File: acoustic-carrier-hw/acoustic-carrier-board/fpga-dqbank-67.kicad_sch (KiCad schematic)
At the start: 11 parts, among them IC1 ECP5-BGA256, Y601 Crystal Oscillator

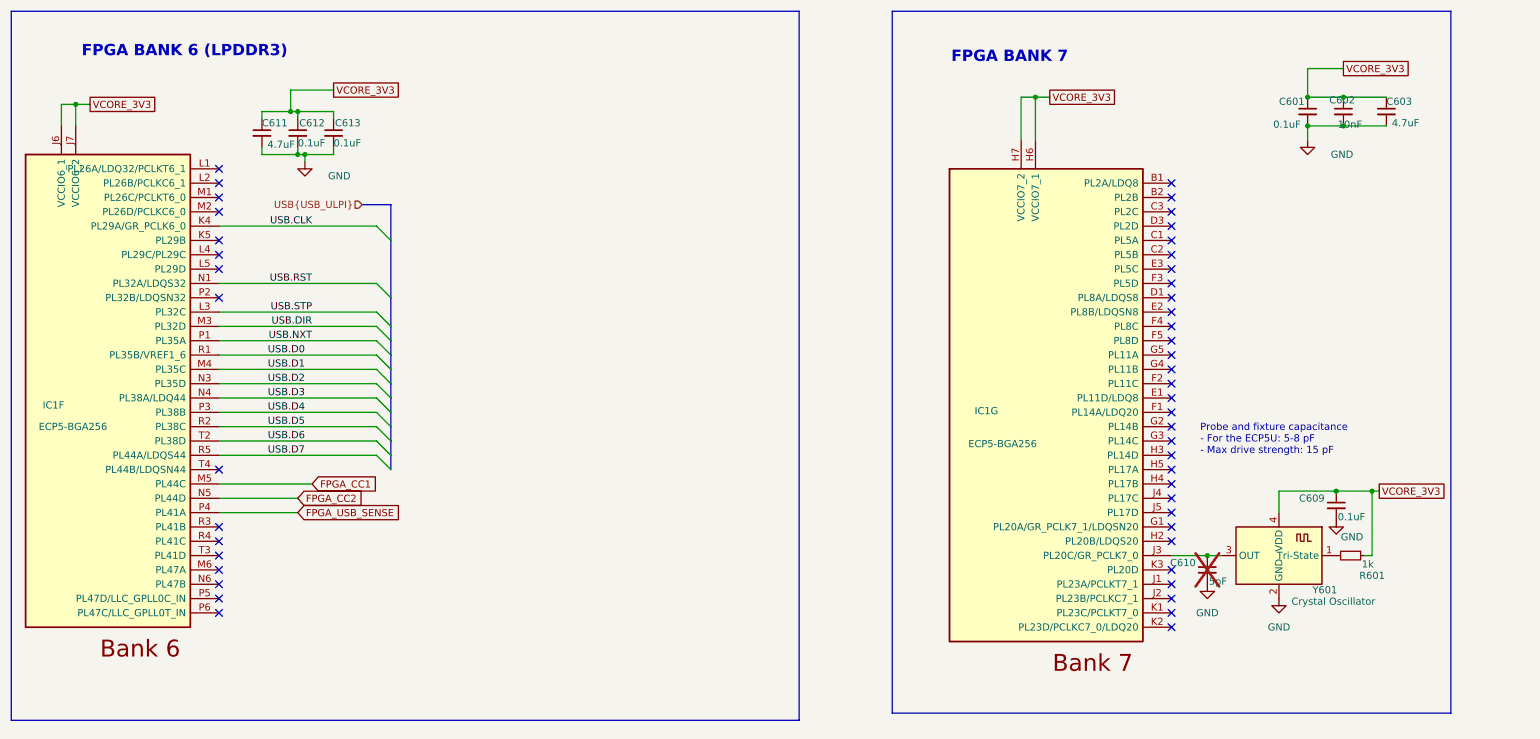
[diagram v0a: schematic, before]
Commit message: [carrier] connected ethernet, usb and adc to appropriate banks, redpositioned schmitt trigger and USB
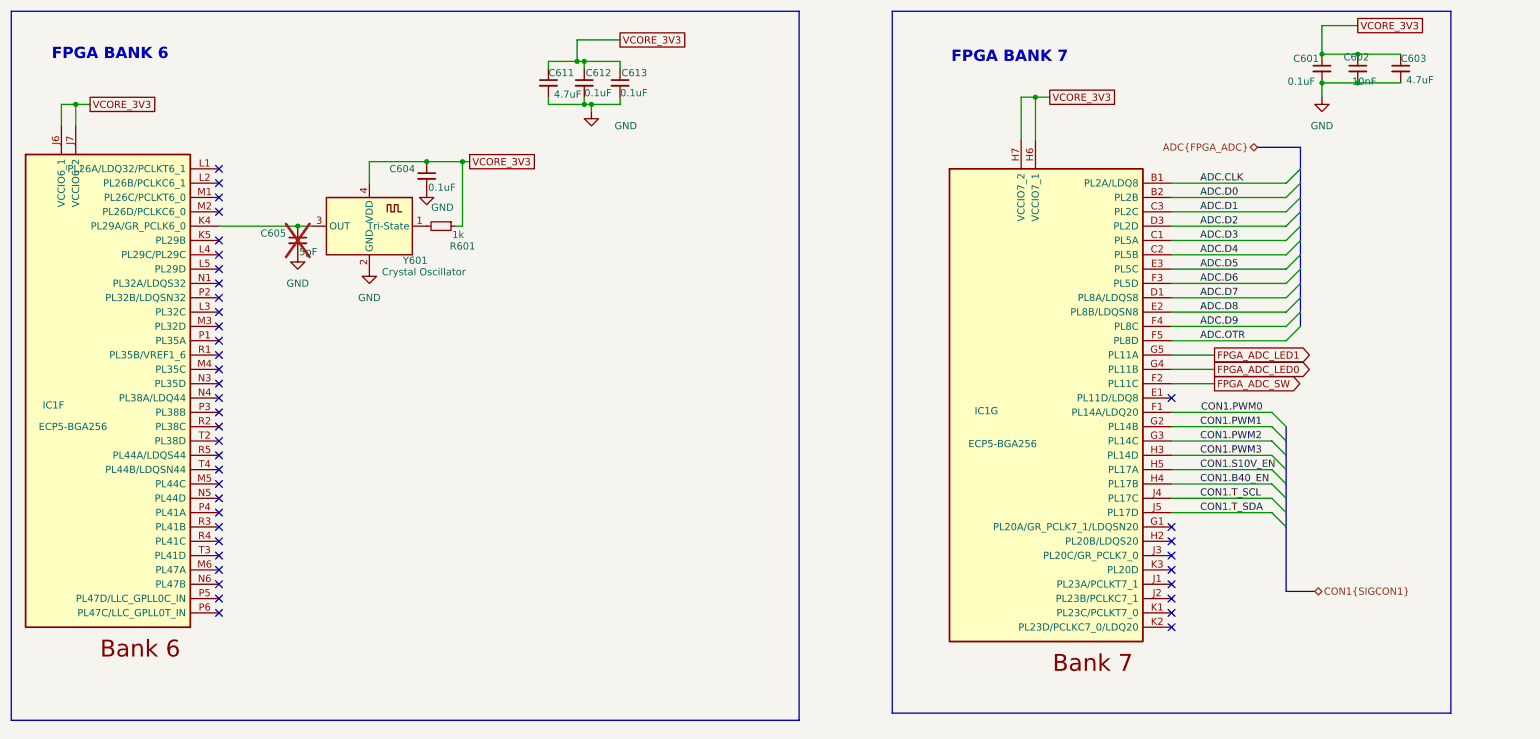
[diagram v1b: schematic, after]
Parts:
- removed C609: 0.1uF, Capacitor_SMD:C_0201_0603Metric, symbol Device:C_Small
- removed C610: 5pF, Capacitor_SMD:C_0603_1608Metric, symbol Device:C_Small
- added C604: 0.1uF, Capacitor_SMD:C_0201_0603Metric, symbol Device:C_Small
- added C605: 5pF, Capacitor_SMD:C_0603_1608Metric, symbol Device:C_Small
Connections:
- net USB.CLK is gone; now on an unnamed net: IC1.K4 (PL29A/GR_PCLK6_0)
- net GND: now also C604.2, C605.2
- net VCORE_3V3: now also C604.1
- net ADC.CLK: now reaches IC1.B1 (PL2A/LDQ8)
- net ADC.D0: now reaches IC1.B2 (PL2B)
- net ADC.D3: now reaches IC1.C1 (PL5A)
- net ADC.D4: now reaches IC1.C2 (PL5B)
- net ADC.D1: now reaches IC1.C3 (PL2C)
- net ADC.D7: now reaches IC1.D1 (PL8A/LDQS8)
- net ADC.D2: now reaches IC1.D3 (PL2D)
- net ADC.D8: now reaches IC1.E2 (PL8B/LDQSN8)
- net ADC.D5: now reaches IC1.E3 (PL5C)
- net CON1.PWM0: now reaches IC1.F1 (PL14A/LDQ20)
- net FPGA_ADC_SW: now reaches IC1.F2 (PL11C)
- net ADC.D6: now reaches IC1.F3 (PL5D)
- net ADC.D9: now reaches IC1.F4 (PL8C)
- net ADC.OTR: now reaches IC1.F5 (PL8D)
- net CON1.PWM1: now reaches IC1.G2 (PL14B)
- net CON1.PWM2: now reaches IC1.G3 (PL14C)
- net FPGA_ADC_LED0: now reaches IC1.G4 (PL11B)
- net FPGA_ADC_LED1: now reaches IC1.G5 (PL11A)
- net CON1.PWM3: now reaches IC1.H3 (PL14D)
- net CON1.B40_EN: now reaches IC1.H4 (PL17B)
- net CON1.S10V_EN: now reaches IC1.H5 (PL17A)
- net at Y601.3 (OUT): now also C605.1; no longer IC1.J3 (PL20C/GR_PCLK7_0)
- net CON1.T_SCL: now reaches IC1.J4 (PL17C)
- net CON1.T_SDA: now reaches IC1.J5 (PL17D)
- net FPGA_CC1: no longer names the net of IC1.M5 (PL44C)
- net FPGA_CC2: no longer names the net of IC1.N5 (PL44D)
- net FPGA_USB_SENSE: no longer names the net of IC1.P4 (PL41A)
- net USB.D0: no longer names the net of IC1.R1 (PL35B/VREF1_6)
- net USB.D1: no longer names the net of IC1.M4 (PL35C)
- net USB.D2: no longer names the net of IC1.N3 (PL35D)
- net USB.D3: no longer names the net of IC1.N4 (PL38A/LDQ44)
- net USB.D4: no longer names the net of IC1.P3 (PL38B)
- net USB.D5: no longer names the net of IC1.R2 (PL38C)
- net USB.D6: no longer names the net of IC1.T2 (PL38D)
- net USB.D7: no longer names the net of IC1.R5 (PL44A/LDQS44)
- net USB.DIR: no longer names the net of IC1.M3 (PL32D)
- net USB.NXT: no longer names the net of IC1.P1 (PL35A)
- net USB.RST: no longer names the net of IC1.N1 (PL32A/LDQS32)
- net USB.STP: no longer names the net of IC1.L3 (PL32C)
- no-connect marks 47 -> 40
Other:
- note added: "FPGA BANK 6"
- note removed: "FPGA BANK 6 (LPDDR3)"
- note removed: "Probe and fixture capacitance - For the ECP5U: 5-8 pF - Max drive strength: 15 pF"
- moved on the sheet: C601, C602, C603, C611, C612, C613

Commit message: [¢arrier] Placed decoupling for some banks, placed dc-dc converterss (next) switch dc-dc converter pins around, switch adc-inputs around
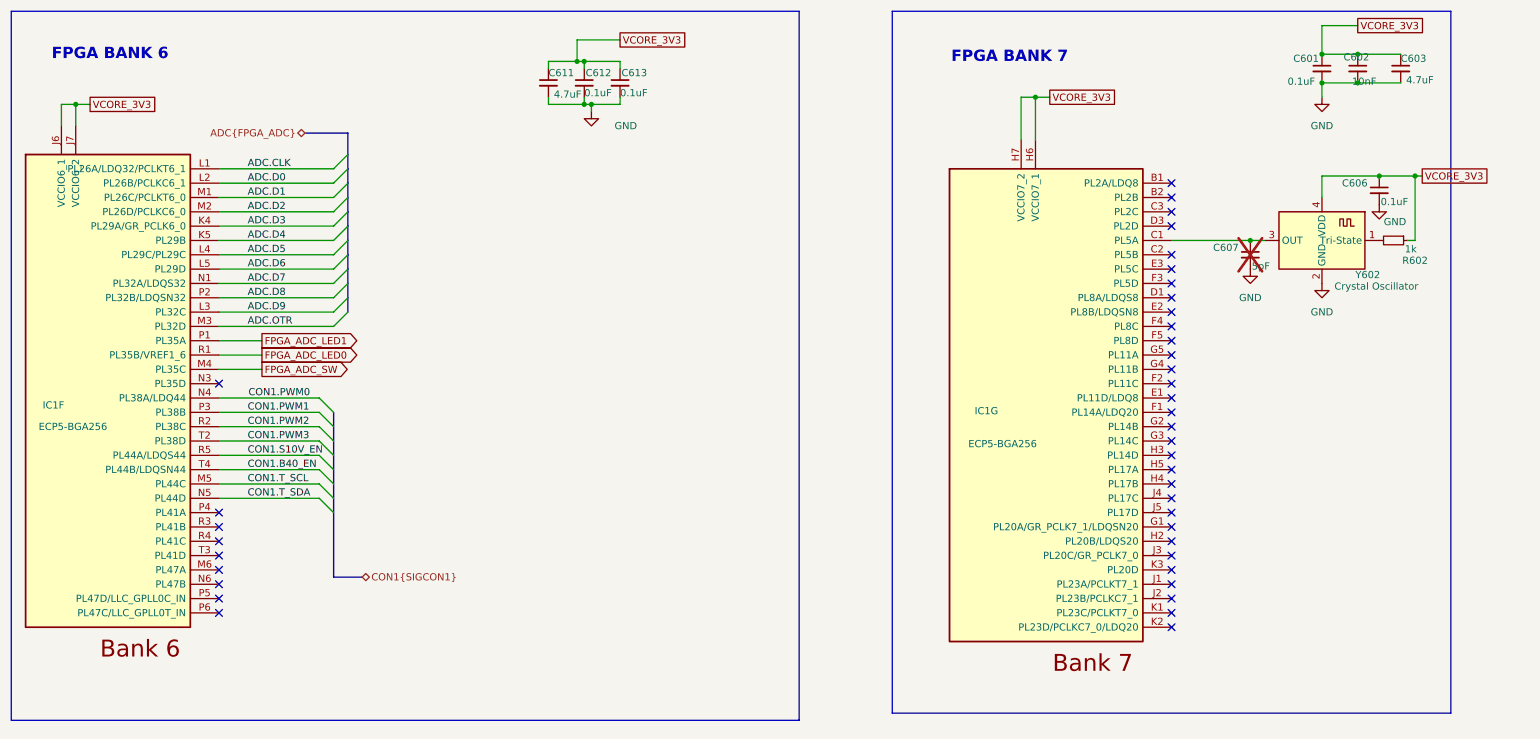
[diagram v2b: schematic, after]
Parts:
- removed C604: 0.1uF, Capacitor_SMD:C_0201_0603Metric, symbol Device:C_Small
- removed C605: 5pF, Capacitor_SMD:C_0603_1608Metric, symbol Device:C_Small
- removed R601: 1k, Resistor_SMD:R_0603_1608Metric, symbol Device:R_Small
- removed Y601: Crystal Oscillator, Crystal:Crystal_SMD_3225-4Pin_3.2x2.5mm, symbol Oscillator:ASCO
- added C606: 0.1uF, Capacitor_SMD:C_0201_0603Metric, symbol Device:C_Small
- added C607: 5pF, Capacitor_SMD:C_0603_1608Metric, symbol Device:C_Small
- added R602: 1k, Resistor_SMD:R_0603_1608Metric, symbol Device:R_Small
- added Y602: Crystal Oscillator, Crystal:Crystal_SMD_3225-4Pin_3.2x2.5mm, symbol Oscillator:ASCO
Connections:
- net ADC.CLK: now also IC1.L1 (PL26A/LDQ32/PCLKT6_1); no longer IC1.B1 (PL2A/LDQ8)
- net ADC.D0: now also IC1.L2 (PL26B/PCLKC6_1); no longer IC1.B2 (PL2B)
- net ADC.D1: now also IC1.M1 (PL26C/PCLKT6_0); no longer IC1.C3 (PL2C)
- net ADC.D2: now also IC1.M2 (PL26D/PCLKC6_0); no longer IC1.D3 (PL2D)
- net ADC.D3: now also IC1.K4 (PL29A/GR_PCLK6_0); no longer IC1.C1 (PL5A)
- net ADC.D4: now also IC1.K5 (PL29B); no longer IC1.C2 (PL5B)
- net ADC.D5: now also IC1.L4 (PL29C/PL29C); no longer IC1.E3 (PL5C)
- net ADC.D6: now also IC1.L5 (PL29D); no longer IC1.F3 (PL5D)
- net ADC.D7: now also IC1.N1 (PL32A/LDQS32); no longer IC1.D1 (PL8A/LDQS8)
- net ADC.D8: now also IC1.P2 (PL32B/LDQSN32); no longer IC1.E2 (PL8B/LDQSN8)
- net ADC.D9: now also IC1.L3 (PL32C); no longer IC1.F4 (PL8C)
- net ADC.OTR: now also IC1.M3 (PL32D); no longer IC1.F5 (PL8D)
- net CON1.B40_EN: now also IC1.T4 (PL44B/LDQSN44); no longer IC1.H4 (PL17B)
- net CON1.PWM0: now also IC1.N4 (PL38A/LDQ44); no longer IC1.F1 (PL14A/LDQ20)
- net CON1.PWM1: now also IC1.P3 (PL38B); no longer IC1.G2 (PL14B)
- net CON1.PWM2: now also IC1.R2 (PL38C); no longer IC1.G3 (PL14C)
- net CON1.PWM3: now also IC1.T2 (PL38D); no longer IC1.H3 (PL14D)
- net CON1.S10V_EN: now also IC1.R5 (PL44A/LDQS44); no longer IC1.H5 (PL17A)
- net CON1.T_SCL: now also IC1.M5 (PL44C); no longer IC1.J4 (PL17C)
- net CON1.T_SDA: now also IC1.N5 (PL44D); no longer IC1.J5 (PL17D)
- net FPGA_ADC_LED0: now also IC1.R1 (PL35B/VREF1_6); no longer IC1.G4 (PL11B)
- net FPGA_ADC_LED1: now also IC1.P1 (PL35A); no longer IC1.G5 (PL11A)
- net FPGA_ADC_SW: now also IC1.M4 (PL35C); no longer IC1.F2 (PL11C)
- net GND: now also C606.2, C607.2, Y602.2 (GND)
- net VCORE_3V3: now also C606.1, R602.1, Y602.4 (VDD)
- new net: R602.2, Y602.1 (Tri-State)
- new net: C607.1, IC1.C1 (PL5A), Y602.3 (OUT)

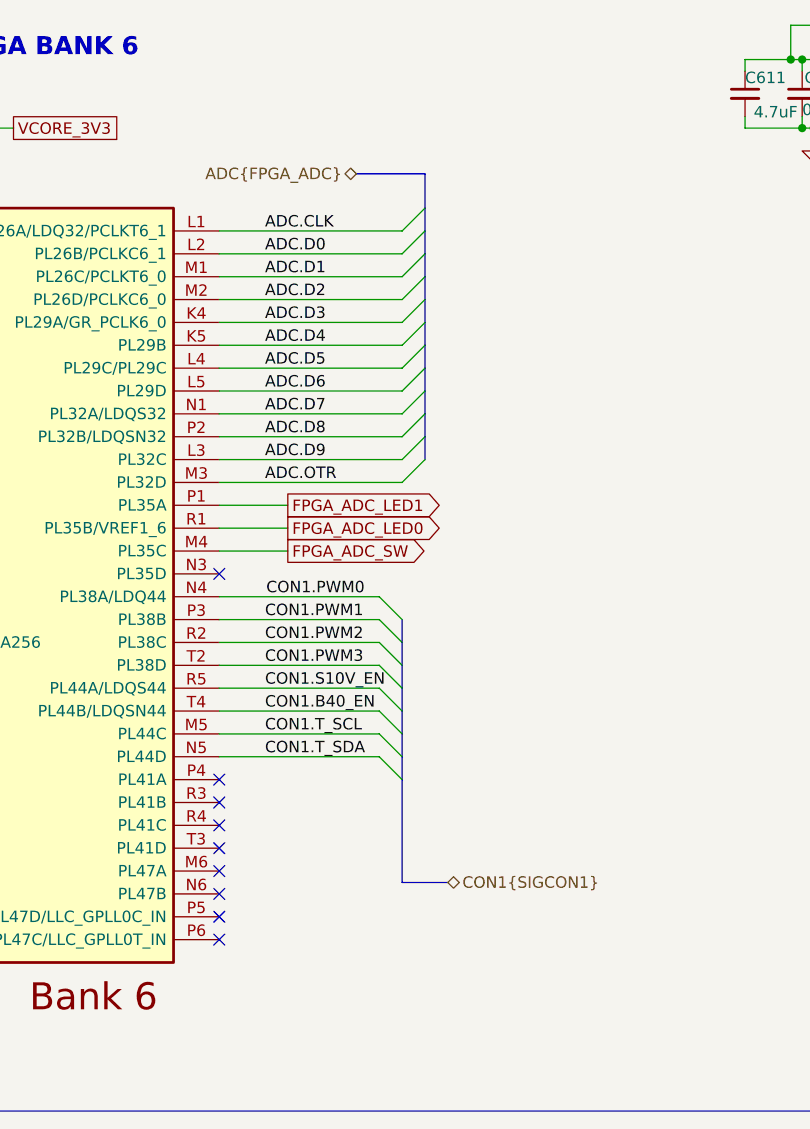
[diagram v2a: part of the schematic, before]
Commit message: [carrier] Rearanged big parts of the analog PCB
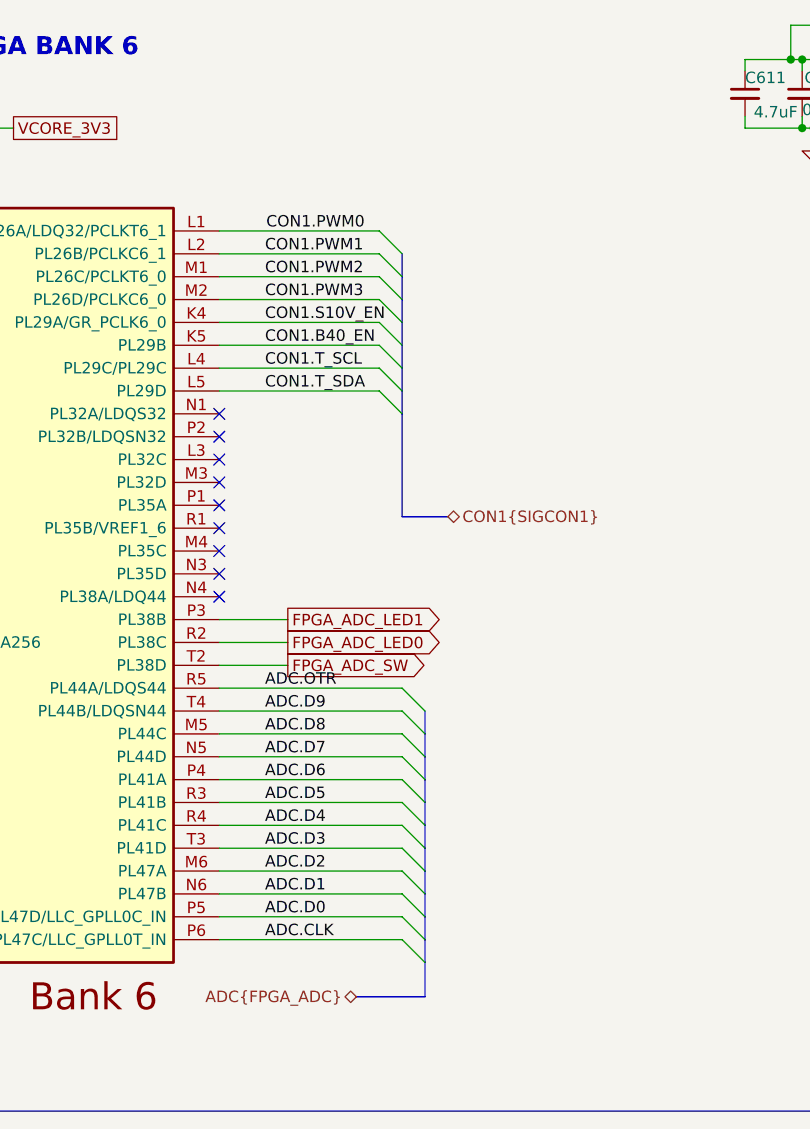
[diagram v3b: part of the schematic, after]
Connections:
- net ADC.CLK: now also IC1.P6 (PL47C/LLC_GPLL0T_IN); no longer IC1.L1 (PL26A/LDQ32/PCLKT6_1)
- net ADC.D0: now also IC1.P5 (PL47D/LLC_GPLL0C_IN); no longer IC1.L2 (PL26B/PCLKC6_1)
- net ADC.D1: now also IC1.N6 (PL47B); no longer IC1.M1 (PL26C/PCLKT6_0)
- net ADC.D2: now also IC1.M6 (PL47A); no longer IC1.M2 (PL26D/PCLKC6_0)
- net ADC.D3: now also IC1.T3 (PL41D); no longer IC1.K4 (PL29A/GR_PCLK6_0)
- net ADC.D4: now also IC1.R4 (PL41C); no longer IC1.K5 (PL29B)
- net ADC.D5: now also IC1.R3 (PL41B); no longer IC1.L4 (PL29C/PL29C)
- net ADC.D6: now also IC1.P4 (PL41A); no longer IC1.L5 (PL29D)
- net ADC.D7: now also IC1.N5 (PL44D); no longer IC1.N1 (PL32A/LDQS32)
- net ADC.D8: now also IC1.M5 (PL44C); no longer IC1.P2 (PL32B/LDQSN32)
- net ADC.D9: now also IC1.T4 (PL44B/LDQSN44); no longer IC1.L3 (PL32C)
- net ADC.OTR: now also IC1.R5 (PL44A/LDQS44); no longer IC1.M3 (PL32D)
- net CON1.B40_EN: now also IC1.K5 (PL29B); no longer IC1.T4 (PL44B/LDQSN44)
- net CON1.PWM0: now also IC1.L1 (PL26A/LDQ32/PCLKT6_1); no longer IC1.N4 (PL38A/LDQ44)
- net CON1.PWM1: now also IC1.L2 (PL26B/PCLKC6_1); no longer IC1.P3 (PL38B)
- net CON1.PWM2: now also IC1.M1 (PL26C/PCLKT6_0); no longer IC1.R2 (PL38C)
- net CON1.PWM3: now also IC1.M2 (PL26D/PCLKC6_0); no longer IC1.T2 (PL38D)
- net CON1.S10V_EN: now also IC1.K4 (PL29A/GR_PCLK6_0); no longer IC1.R5 (PL44A/LDQS44)
- net CON1.T_SCL: now also IC1.L4 (PL29C/PL29C); no longer IC1.M5 (PL44C)
- net CON1.T_SDA: now also IC1.L5 (PL29D); no longer IC1.N5 (PL44D)
- net FPGA_ADC_LED0: now also IC1.R2 (PL38C); no longer IC1.R1 (PL35B/VREF1_6)
- net FPGA_ADC_LED1: now also IC1.P3 (PL38B); no longer IC1.P1 (PL35A)
- net FPGA_ADC_SW: now also IC1.T2 (PL38D); no longer IC1.M4 (PL35C)
